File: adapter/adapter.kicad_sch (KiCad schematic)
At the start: 22 parts, among them J10 Ribbon, J11 Ribbon, J12 Ribbon, J13 serial, J14 serial, J3 battery charge, J6 battery charge, J7 trackball, J8 trackball, J9 Ribbon, SW1 SW_SPST, SW2 SW_SPST, SW3 SW_SPDT, SW4 SW_SPDT, U1 eliteC, U2 eliteC

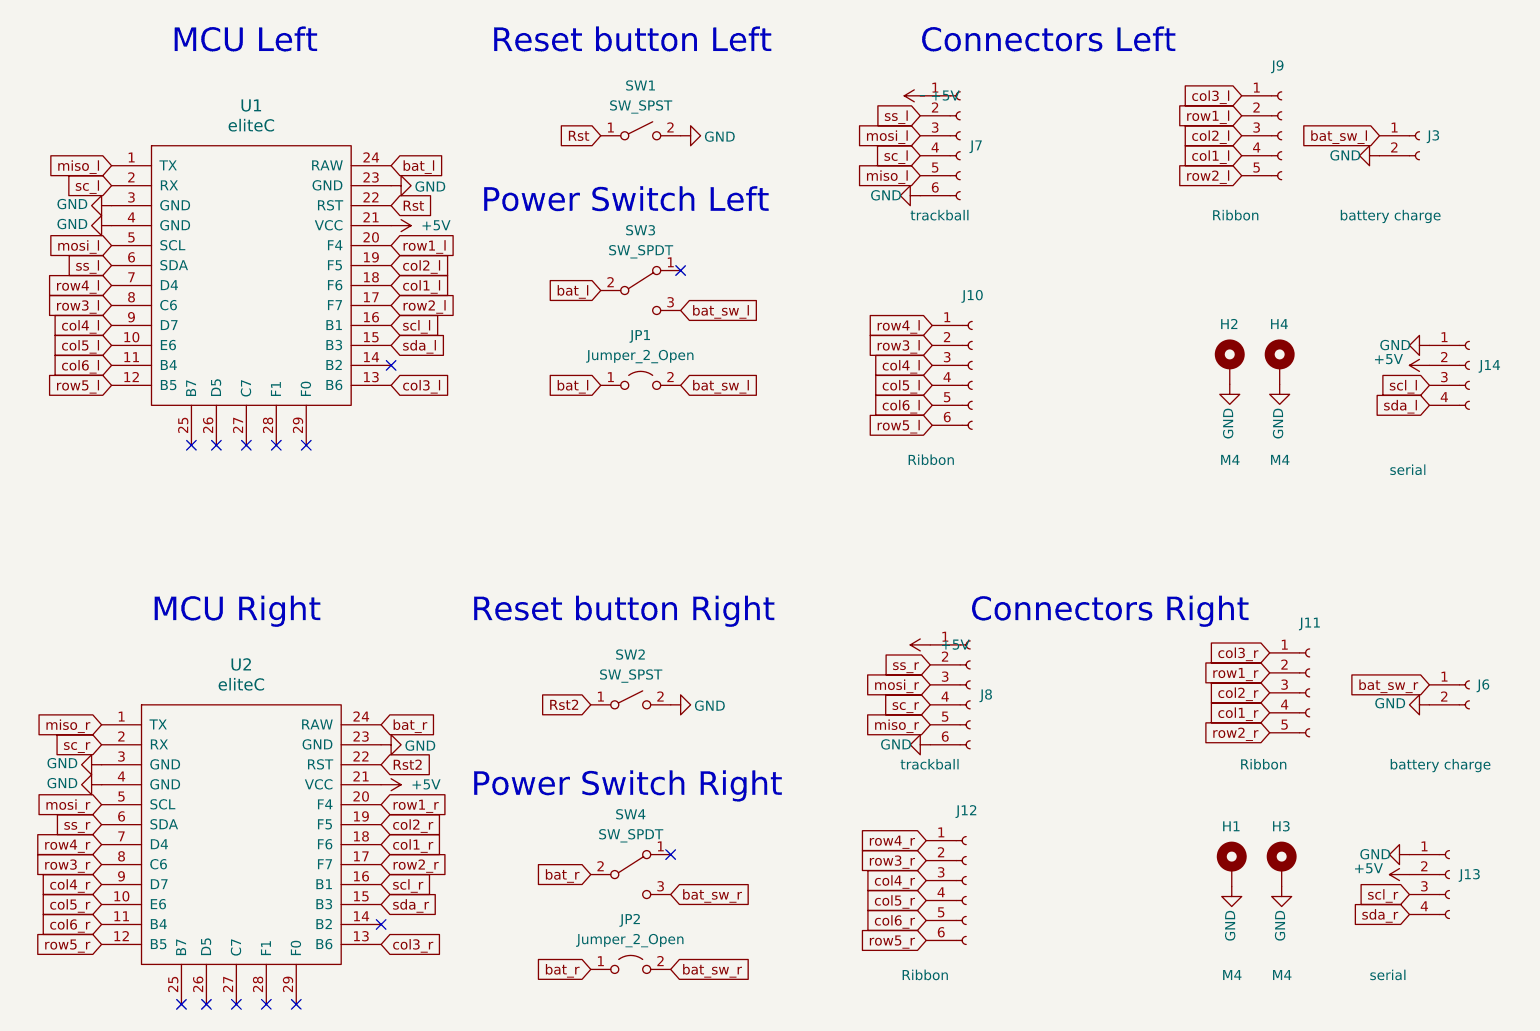
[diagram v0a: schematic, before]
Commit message: remove fill and unused serial connectors
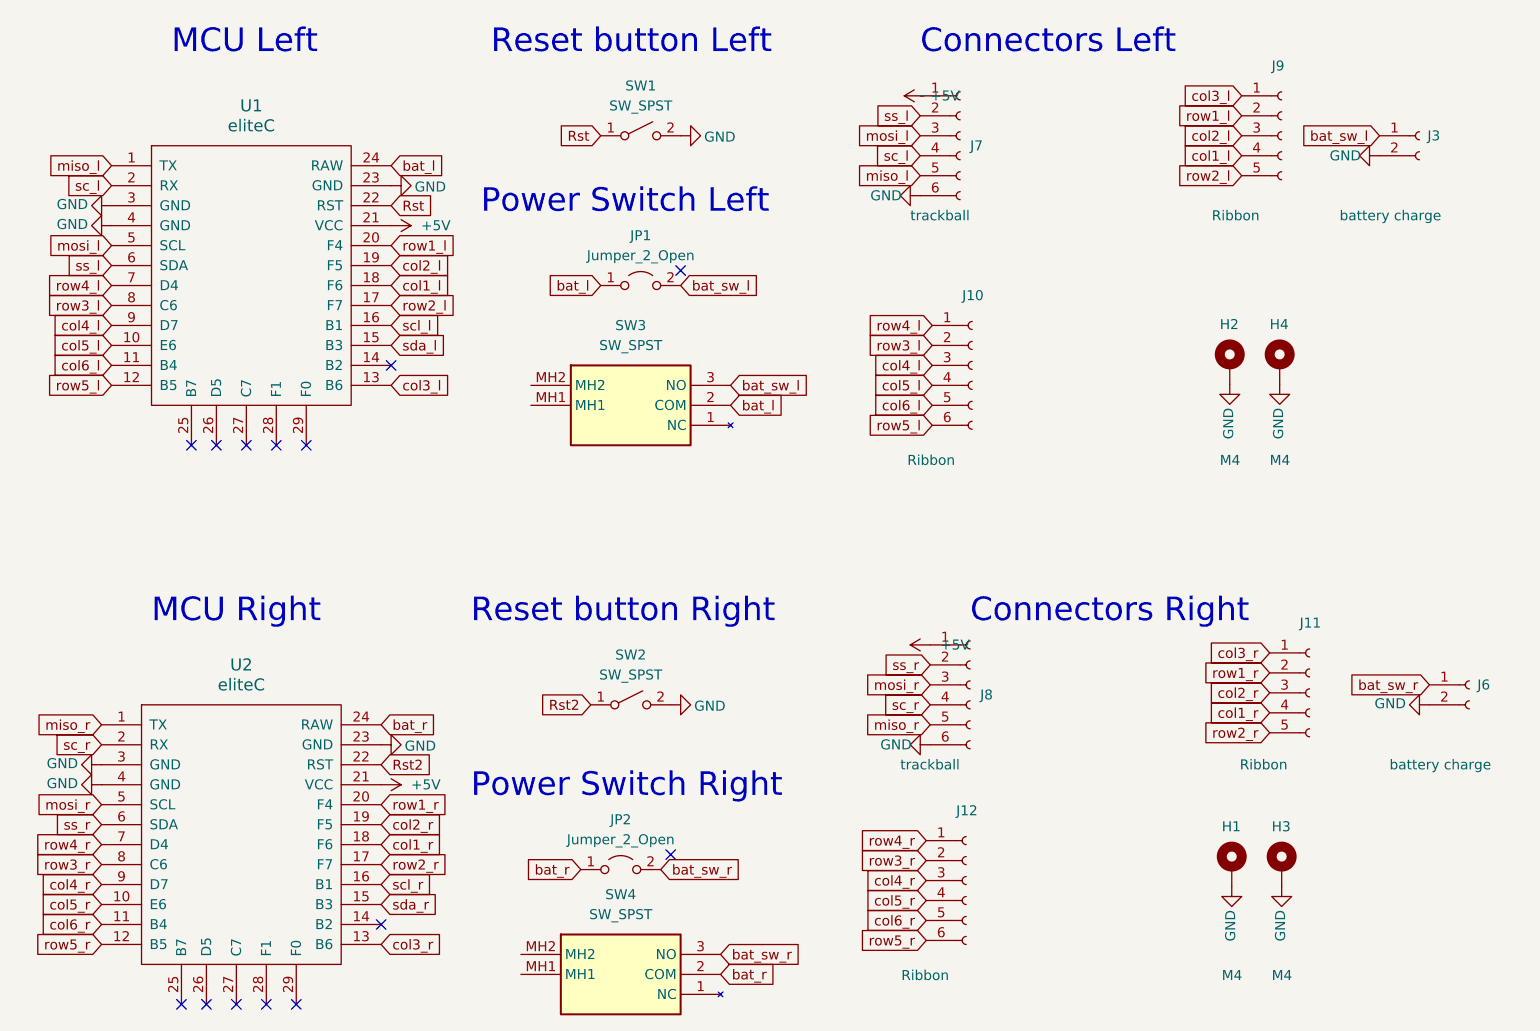
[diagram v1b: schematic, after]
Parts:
- removed J13, J14: serial, Library:PinHeader_1x04_P2.54mm_Vertical, symbol Connector:Conn_01x04_Female
- removed SW3, SW4: SW_SPDT, Library:SW_SPDT+H-MSK12C01_hor(7pin_SMD), symbol Switch:SW_SPDT
- added SW3, SW4: SW_SPST, 200AWMSP2T2A1M6RE, symbol 200AWMSP2T2A1M6RE:200AWMSP2T2A1M6RE
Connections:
- net bat_l: now also SW3.2 (COM)
- net bat_r: now also SW4.2 (COM)
- net bat_sw_l: now also SW3.3 (NO)
- net bat_sw_r: now also SW4.3 (NO)
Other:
- moved on the sheet: JP1, JP2

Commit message: simplify
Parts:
- removed JP1, JP2: Jumper_2_Open, Library:power_switch_jumper, symbol Jumper:Jumper_2_Open
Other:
- moved on the sheet: SW3, SW4
